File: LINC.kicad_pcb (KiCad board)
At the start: 4 copper layers, 55.1 x 58 mm, 44 parts, among them J1 112-024-113R001, J2 FTSH-105-01-L-DV-K, J3 RJHSE5380, J4 USB4085-GF-A, U1 SN74LVC8T245PWR, U2 SN74LVC07APWR, U3 STM32H533RETx, U4 PTS645SH43SMTR92 LFS, U5 THVD1451D, U6 SN74LVC1G07DCKR, U7 SN74LVC14APWR, U8 USBLC6-2SC6, U9 TPSM861253RDXR, Y1 MU00525-32.768K, Y2 CS10820-24M

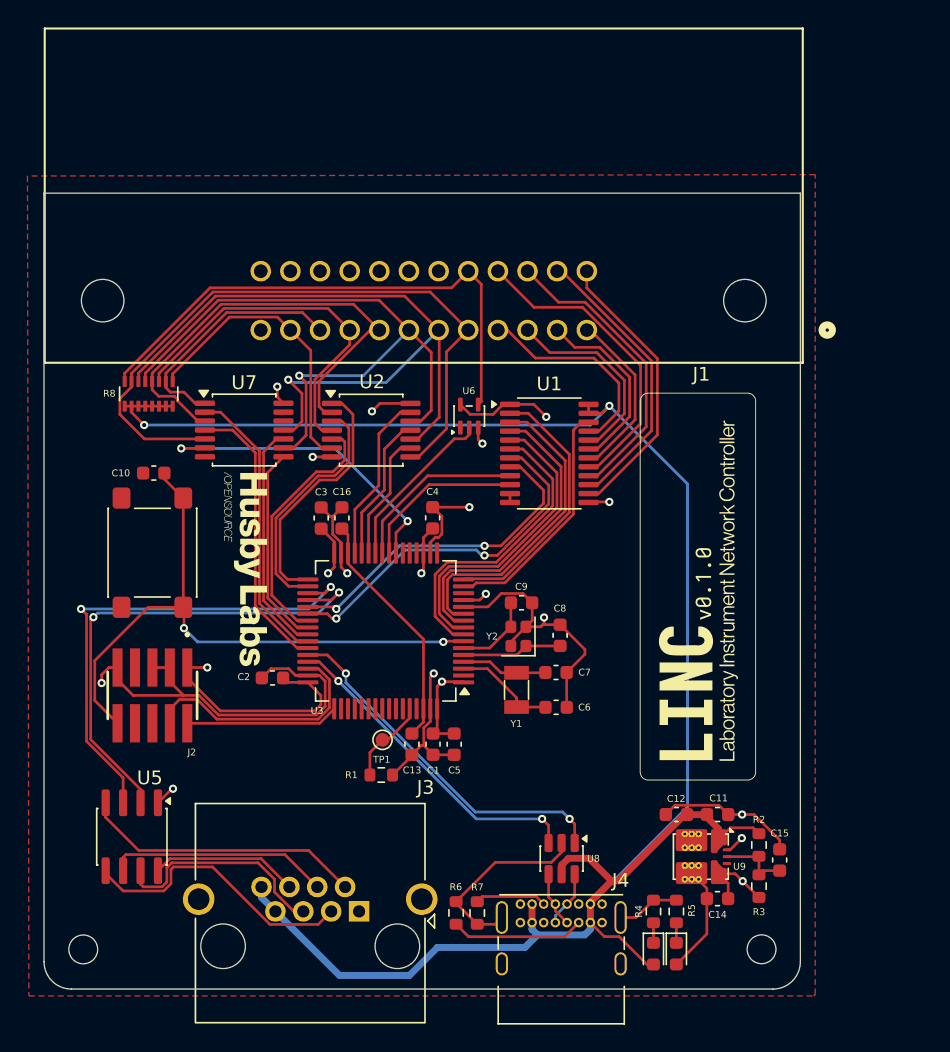
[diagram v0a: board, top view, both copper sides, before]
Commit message: Migrate to LDO for 3V3
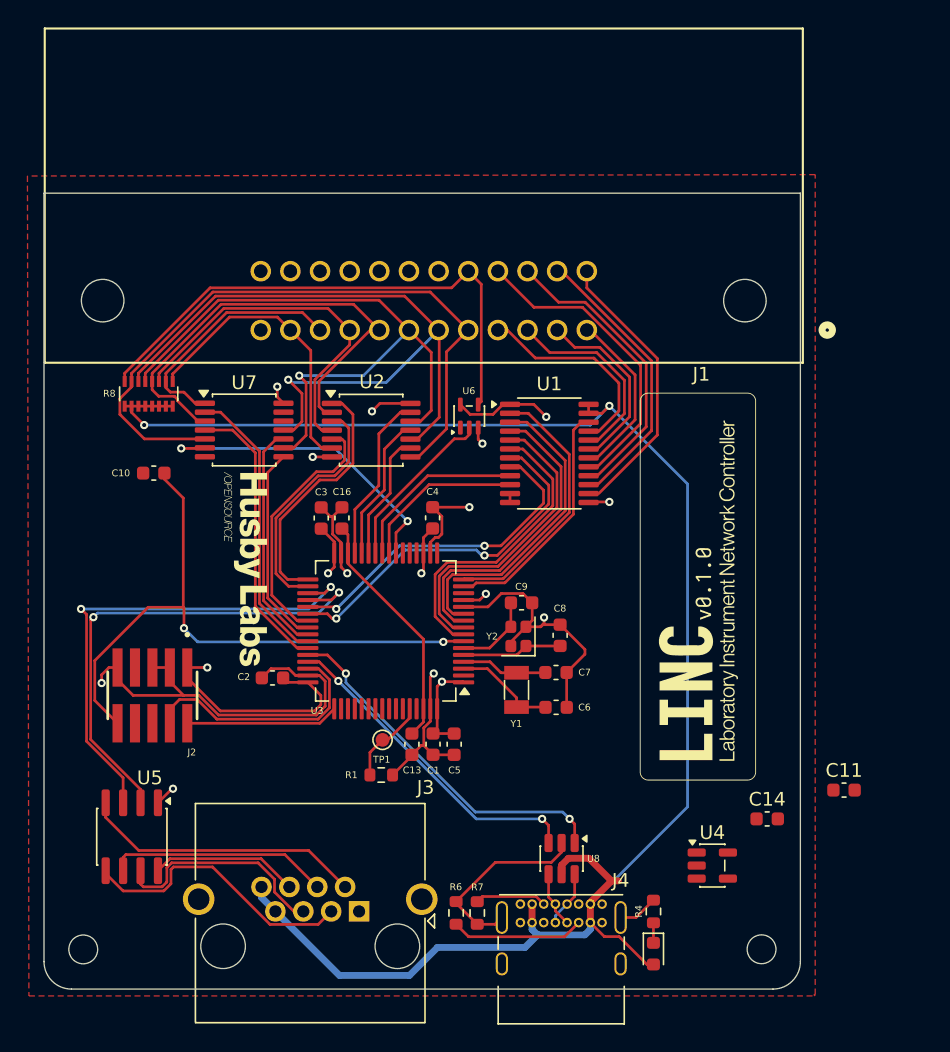
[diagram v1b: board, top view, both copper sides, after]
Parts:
- removed C12: 10 µF, Capacitor_SMD:C_0603_1608Metric
- removed C15: 10000 pF, Capacitor_SMD:C_0603_1608Metric
- removed D2: Red, LED_SMD:LED_0603_1608Metric
- removed R2: 15.8k, Resistor_SMD:R_0603_1608Metric
- removed R3: 10k, Resistor_SMD:R_0603_1608Metric
- removed R5: 68, Resistor_SMD:R_0603_1608Metric
- removed U9: TPSM861253RDXR, Package_DFN_QFN:Texas_RDX0007A_QFN-FCMOD-7-3.3x4mm-P0.5mm_4EP
- C11: value 100nF -> 1 µF
- C14: value 22 µF -> 2.2 µF
- U4: value PTS645SH43SMTR92 LFS -> TLV74311PDBVR; footprint Button_Switch_SMD:SW_SPST_PTS645Sx43SMTR92 -> Package_TO_SOT_SMD:SOT-23-5
- moved U4 46.7 mm to (185.8, 114.8), turned to 0 degrees
- moved C11 9.39 mm to (195.4, 109.3)
- moved C14 6.85 mm to (189.8, 111.4)
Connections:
- U4 pad 1: Net-(J2-NRST) -> +5V
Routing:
- net GND: track 136.3 -> 118.6 mm, vias 10 -> 8
- net +5V: track 144.5 -> 130.3 mm
- net +3V3: track 56.5 -> 47.0 mm, vias 10 -> 9
- net Net-(U9-EN): track 5.33 -> 0.00 mm
- net Net-(D2-K): track 1.46 -> 0.00 mm

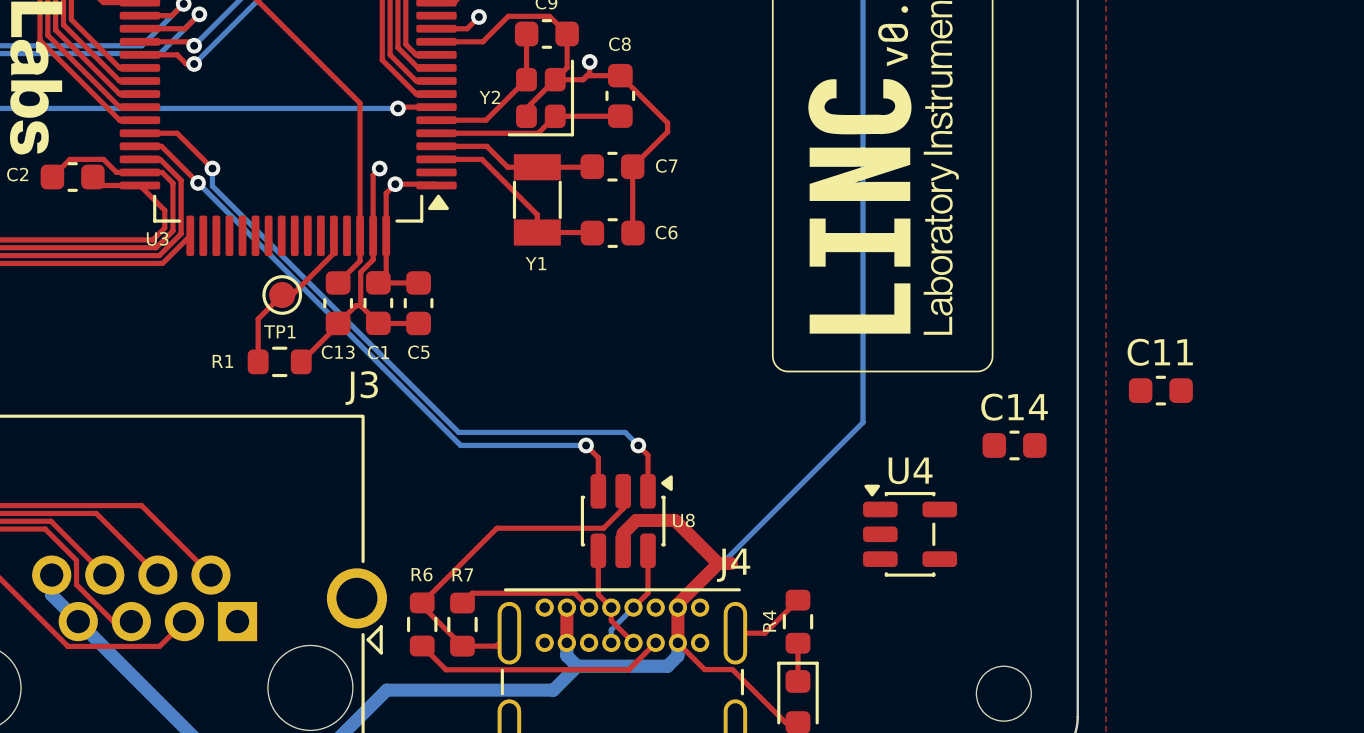
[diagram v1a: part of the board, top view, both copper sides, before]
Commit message: Update STM32 symbol
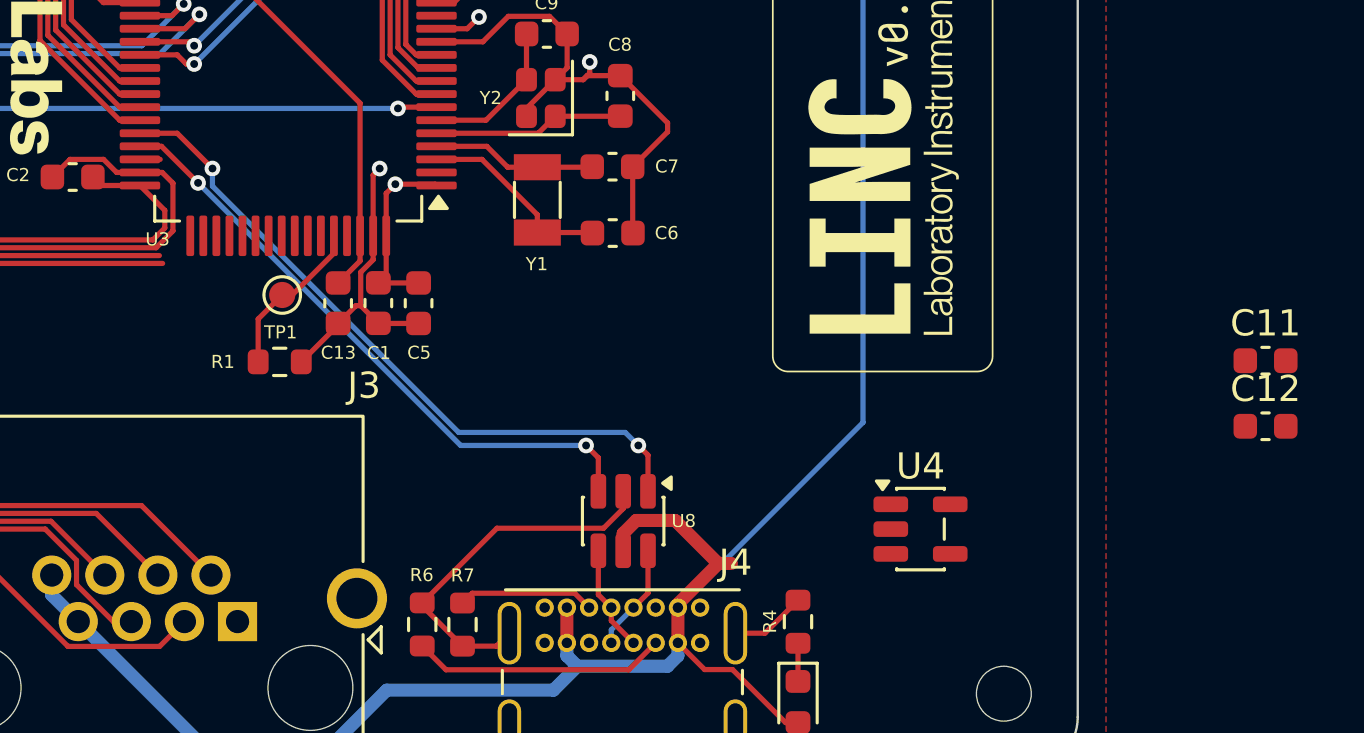
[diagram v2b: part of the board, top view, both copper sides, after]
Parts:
- removed C14: 2.2 µF, Capacitor_SMD:C_0603_1608Metric
- added C12: 4.7 µF, Capacitor_SMD:C_0603_1608Metric, F.Cu at (199.4, 110.6)
- C11: value 1 µF -> 4.7 µF
- U3: value STM32H533RETx -> STM32H523RETx
- moved C11 4.17 mm to (199.4, 108.1)
- moved U4 0.45 mm to (186.2, 114.6)
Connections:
- U3 pad 46: Net-(J2-SWCLK) -> Net-(J2-SWDIO)
- U3 pad 49: Net-(J2-SWDIO) -> Net-(J2-SWCLK)
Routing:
- net Net-(J2-SWCLK): track 17.8 -> 12.7 mm
- net Net-(J2-SWDIO): track 11.1 -> 10.4 mm

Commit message: Implement SWO async tracing
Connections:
- J2 pad 06: unconnected-(J2-SWO-Pad06) -> Net-(J2-SWO)
- U3 pad 55: unconnected-(U3H-PB3(JTDO)-Pad55) -> Net-(J2-SWO)
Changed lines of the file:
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@@
 			(unit
 				(name "B")
-				(pins "3" "4" "5" "6" "46" "49" "60" "7")
+				(pins "3" "4" "5" "6" "46" "49" "55" "60" "7")
 			)
 			(unit
@@
 			(unit
 				(name "H")
-				(pins "15" "20" "41" "42" "43" "50" "26" "27" "28" "55" "56" "57" "58"
-					"8" "9" "10" "11" "24" "25" "37" "38" "39" "40" "51" "52" "53" "2" "54"
+				(pins "15" "20" "41" "42" "43" "50" "26" "27" "28" "56" "57" "58" "8"
+					"9" "10" "11" "24" "25" "37" "38" "39" "40" "51" "52" "53" "2" "54"
 				)
 			)
@@
 			(layers "F.Cu" "F.Mask" "F.Paste")
 			(roundrect_rratio 0.25)
-			(net "unconnected-(U3H-PB3(JTDO)-Pad55)")
-			(pinfunction "PB3(JTDO)_55")
-			(pintype "bidirectional+no_connect")
+			(net "Net-(J2-SWO)")
+			(pinfunction "PB3-JTDO/SWO_55")
+			(pintype "bidirectional")
 		)
 		(pad "56" smd roundrect
@@
 			(size 0.7366 2.794)
 			(layers "F.Cu" "F.Mask" "F.Paste")
-			(net "unconnected-(J2-SWO-Pad06)")
+			(net "Net-(J2-SWO)")
 			(pinfunction "SWO_06")
-			(pintype "passive+no_connect")
+			(pintype "passive")
 			(solder_mask_margin 0.102)
 		)
@@
 	)
 	(segment
+		(start 147.530501 104.398398)
+		(end 157.183501 104.398398)
+		(width 0.2)
+		(layer "F.Cu")
+		(net "Net-(J2-SWDIO)")
+	)
+	(segment
+		(start 156.315501 100.416398)
+		(end 157.0905 100.416398)
+		(width 0.2)
+		(layer "F.Cu")
+		(net "Net-(J2-SWDIO)")
+	)
+	(segment
 		(start 148.258501 102.666398)
 		(end 146.963801 102.666398)
@@
 	)
 	(segment
-		(start 147.530501 104.398398)
-		(end 157.183501 104.398398)
-		(width 0.2)
-		(layer "F.Cu")
-		(net "Net-(J2-SWDIO)")
-	)
-	(segment
-		(start 156.315501 100.416398)
-		(end 157.0905 100.416398)
-		(width 0.2)
-		(layer "F.Cu")
-		(net "Net-(J2-SWDIO)")
-	)
-	(segment

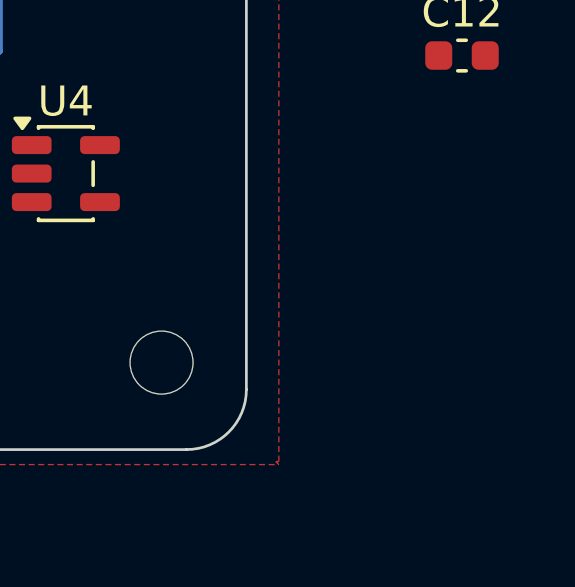
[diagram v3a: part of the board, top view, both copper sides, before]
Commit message: Change PWR LED to 1k current limiting
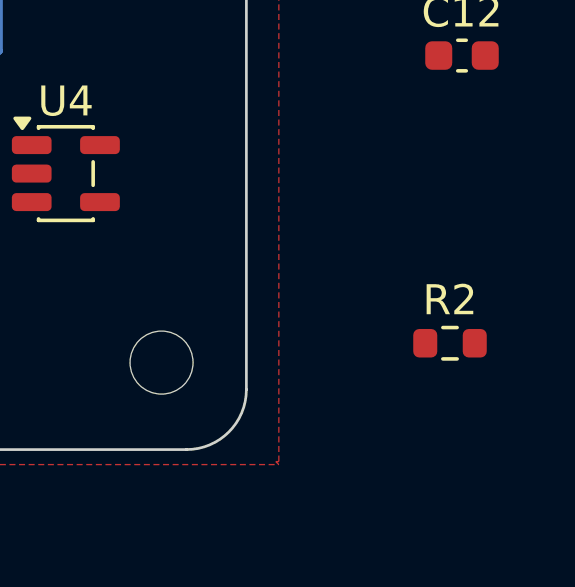
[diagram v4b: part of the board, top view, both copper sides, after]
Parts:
- added R2: 1k, Resistor_SMD:R_0603_1608Metric, F.Cu at (199.0, 120.2)

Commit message: Update layout
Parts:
- removed R4: 150, Resistor_SMD:R_0603_1608Metric
- moved C10 20.9 mm to (151.6, 106.1), turned to 0 degrees
- moved C11 17.9 mm to (182.6, 114.3), turned to -90 degrees
- moved R2 17.6 mm to (181.5, 118.0), turned to 90 degrees
- moved C12 11.7 mm to (188.3, 114.3), turned to -90 degrees
- moved U4 0.81 mm to (185.5, 114.2)
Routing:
- net Net-(J2-SWO): track 0.00 -> 19.5 mm
- net Net-(J2-NRST): track 46.0 -> 33.4 mm
- net Net-(J2-SWDIO): track 10.4 -> 16.9 mm
- net GND: track 118.6 -> 120.7 mm
- net +5V: track 130.3 -> 132.1 mm, vias 2 -> 3
- net Net-(J2-SWCLK): track 12.7 -> 14.4 mm
- net +3V3: vias 9 -> 11
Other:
- board text added: "PWR"
- board text removed: "3V3"
- board text removed: "5V"

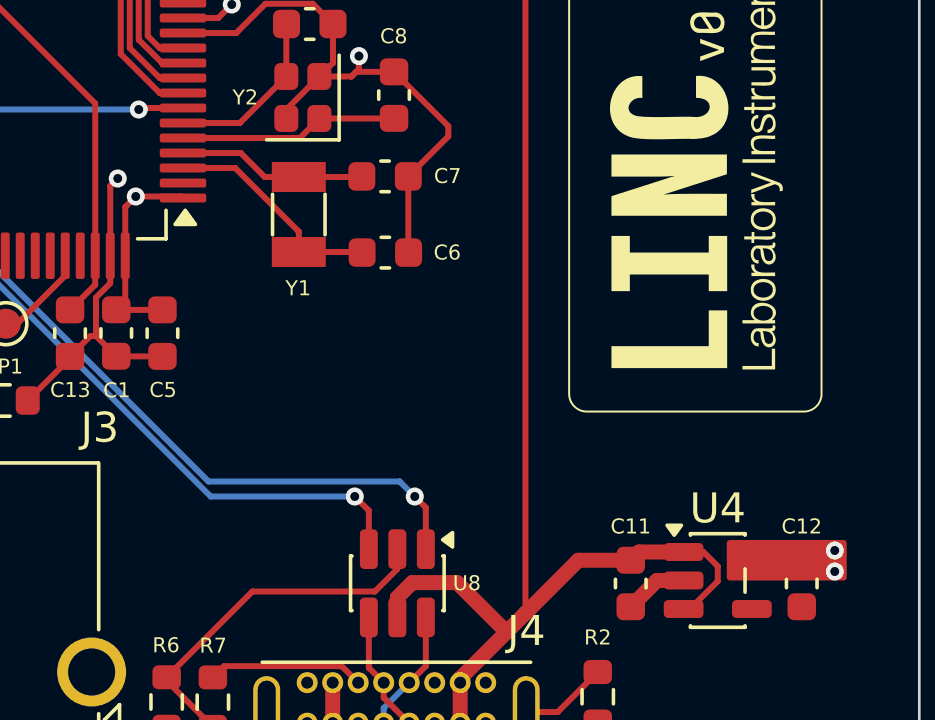
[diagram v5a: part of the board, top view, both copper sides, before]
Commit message: Add and layout LED
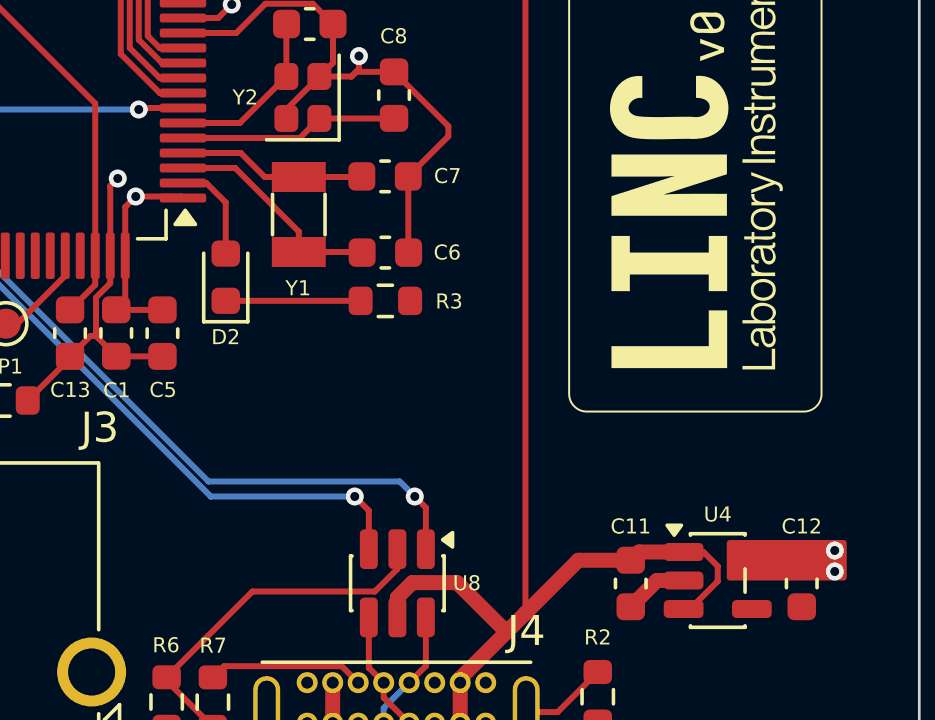
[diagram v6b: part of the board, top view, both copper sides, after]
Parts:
- added D2: Red, LED_SMD:LED_0603_1608Metric, F.Cu at (169.1, 104.1)
- added R3: 1k, Resistor_SMD:R_0603_1608Metric, F.Cu at (174.4, 104.8)
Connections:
- U3 pad 2: unconnected-(U3H-PC13-Pad2) -> Net-(D2-A)
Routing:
- net Net-(D2-K): track 0.00 -> 4.50 mm
- net Net-(D2-A): track 0.00 -> 3.40 mm
